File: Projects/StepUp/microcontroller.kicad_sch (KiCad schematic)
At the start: 34 parts, among them J1 USB_C_Receptacle_USB2.0_16P, J2 Conn_01x02, J3 Conn_02x03_Odd_Even, J4 Conn_02x06_Odd_Even, SW1 FSM8JSMASTR, SW2 FSM8JSMASTR, SW3 FSM8JSMASTR, U1 USBLC6-2SC6, U2 W25Q128JVS, U3 RP2040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

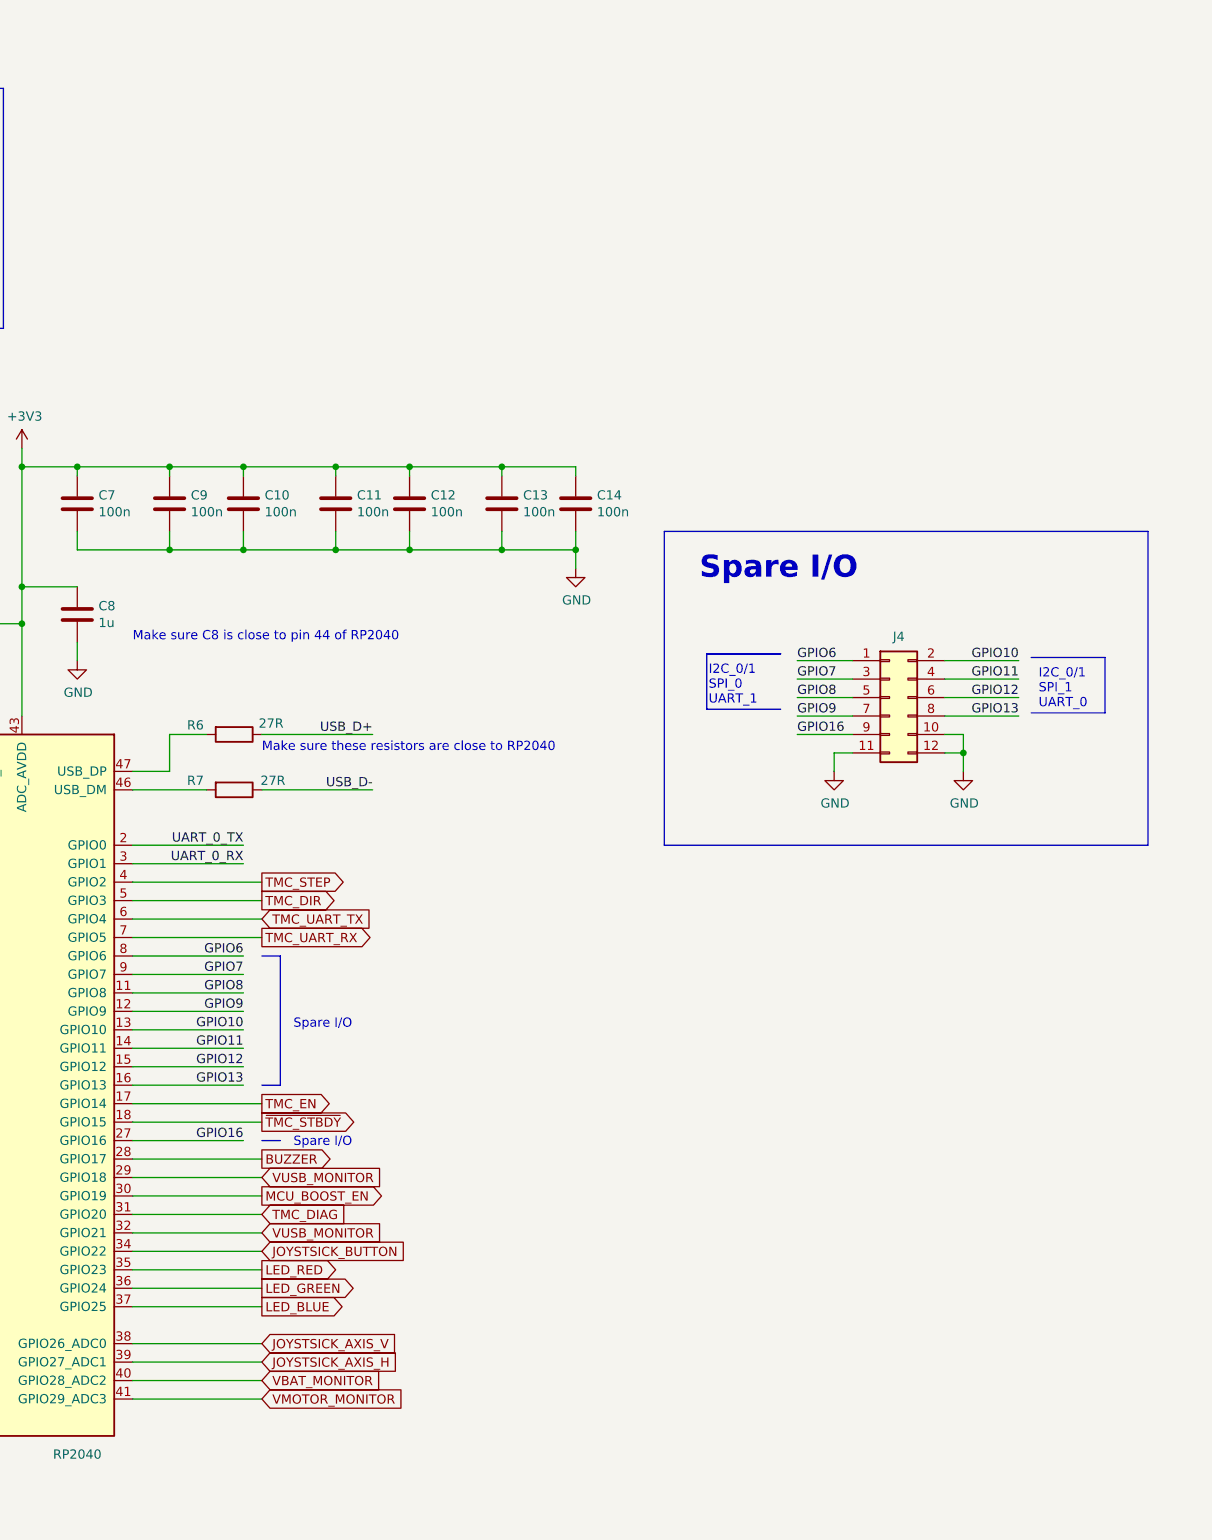
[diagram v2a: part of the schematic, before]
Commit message: feat(layout): DRC ongoing, layout nearly complete
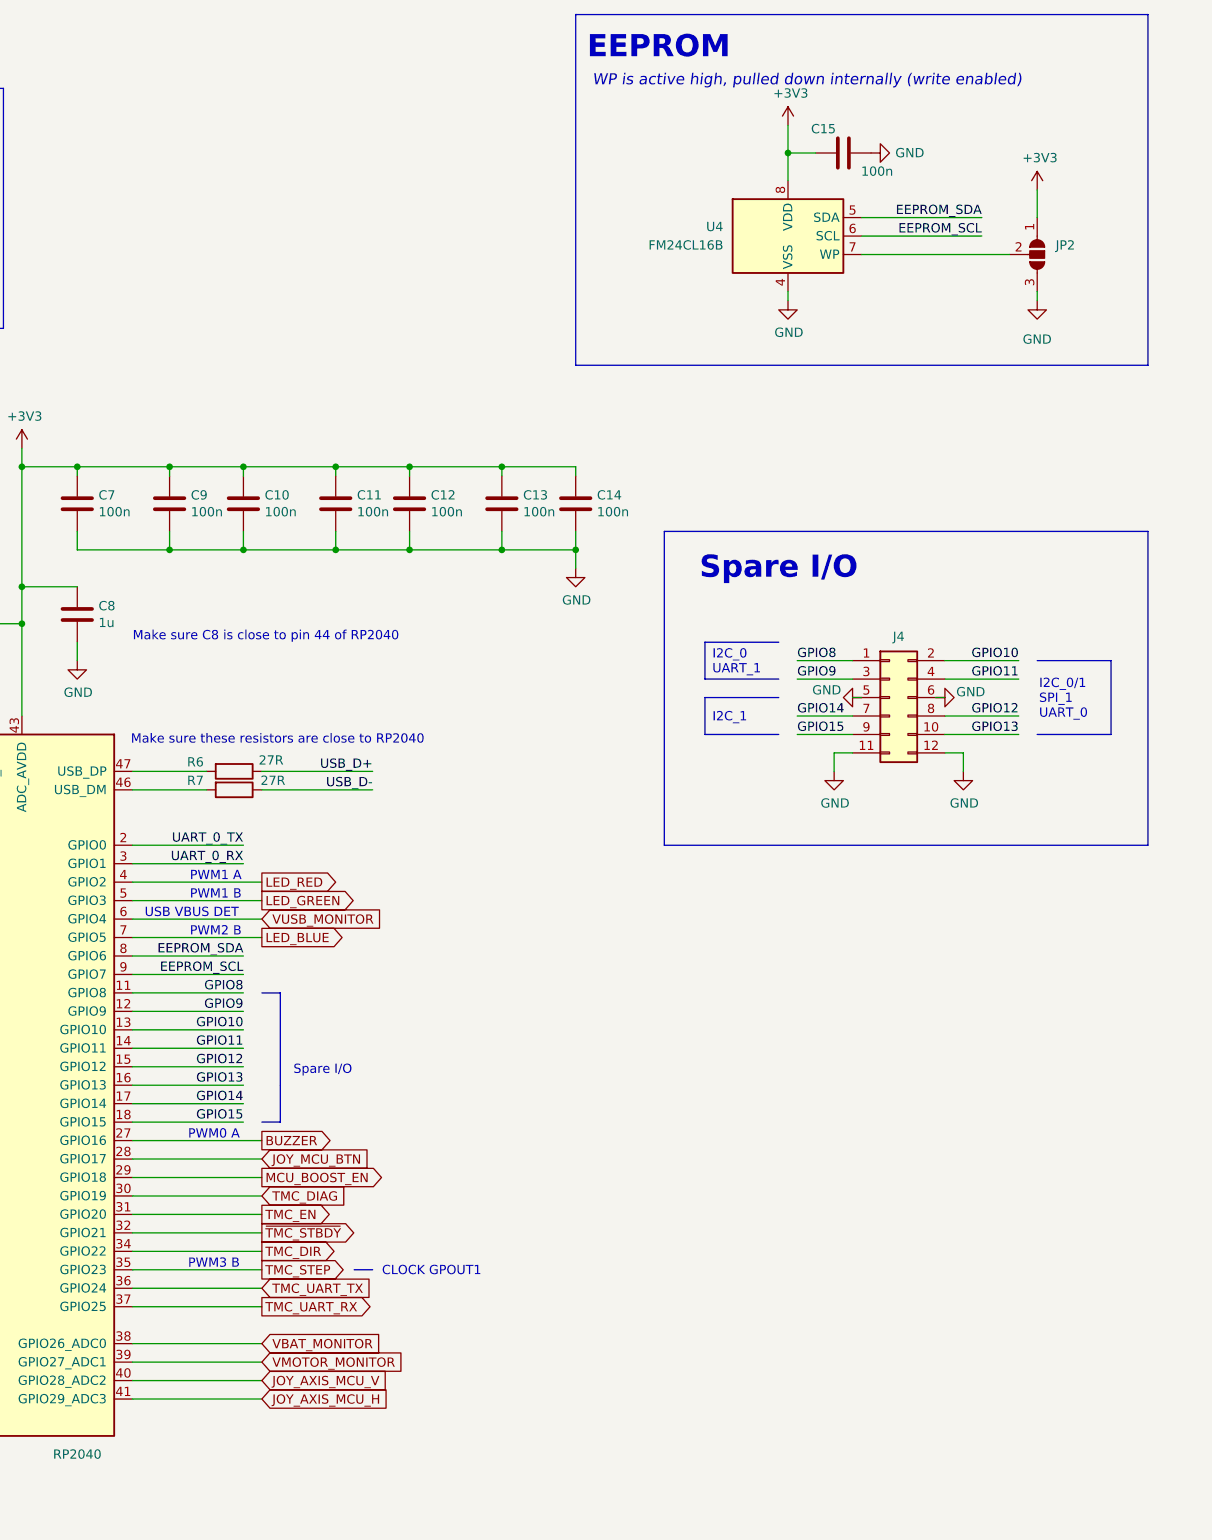
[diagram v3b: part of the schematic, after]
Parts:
- added C15: 100n, Capacitor_SMD:C_0402_1005Metric, symbol Device:C
- added JP2: SolderJumper_3_Open, Jumper:SolderJumper-3_P1.3mm_Bridged12_RoundedPad1.0x1.5mm, symbol Jumper:SolderJumper_3_Open
- added U4: FM24CL16B, Package_SO:SOIC-8_3.9x4.9mm_P1.27mm, symbol Memory_NVRAM:FM24CL16B
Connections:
- net JOYSTSICK_AXIS_H is gone; now on net VMOTOR_MONITOR: U3.39 (GPIO27_ADC1)
- net JOYSTSICK_AXIS_V is gone; now on net VBAT_MONITOR: U3.38 (GPIO26_ADC0)
- net JOYSTSICK_BUTTON is gone; now on net TMC_DIR: U3.34 (GPIO22)
- net +3V3: now also C15.1, JP2.1 (A), U4.8 (VDD)
- net BUZZER: now also U3.27 (GPIO16); no longer U3.28 (GPIO17)
- net GND: now also J4.5 (Pin_5), J4.6 (Pin_6), C15.2, JP2.3 (B), U4.4 (VSS); no longer J4.10 (Pin_10)
- net GPIO12: now also J4.8 (Pin_8); no longer J4.6 (Pin_6)
- net GPIO13: now also J4.10 (Pin_10); no longer J4.8 (Pin_8)
- net GPIO8: now also J4.1 (Pin_1); no longer J4.5 (Pin_5)
- net GPIO9: now also J4.3 (Pin_3); no longer J4.7 (Pin_7)
- net LED_BLUE: now also U3.7 (GPIO5); no longer U3.37 (GPIO25)
- net LED_GREEN: now also U3.5 (GPIO3); no longer U3.36 (GPIO24)
- net LED_RED: now also U3.4 (GPIO2); no longer U3.35 (GPIO23)
- net MCU_BOOST_EN: now also U3.29 (GPIO18); no longer U3.30 (GPIO19)
- net TMC_DIAG: now also U3.30 (GPIO19); no longer U3.31 (GPIO20)
- net TMC_DIR: no longer U3.5 (GPIO3)
- net TMC_EN: now also U3.31 (GPIO20); no longer U3.17 (GPIO14)
- net TMC_STEP: now also U3.35 (GPIO23); no longer U3.4 (GPIO2)
- net TMC_UART_RX: now also U3.37 (GPIO25); no longer U3.7 (GPIO5)
- net TMC_UART_TX: now also U3.36 (GPIO24); no longer U3.6 (GPIO4)
- net VBAT_MONITOR: no longer U3.40 (GPIO28_ADC2)
- net VMOTOR_MONITOR: no longer U3.41 (GPIO29_ADC3)
- net VUSB_MONITOR: now also U3.6 (GPIO4); no longer U3.29 (GPIO18), U3.32 (GPIO21)
- net ~{TMC_STBDY}: now also U3.32 (GPIO21); no longer U3.18 (GPIO15)
- net GPIO16 renamed GPIO15
- net GPIO15: now also U3.18 (GPIO15); no longer U3.27 (GPIO16)
- net GPIO6 renamed EEPROM_SDA
- net EEPROM_SDA: now also U4.5 (SDA); no longer J4.1 (Pin_1)
- net GPIO7 renamed EEPROM_SCL
- net EEPROM_SCL: now also U4.6 (SCL); no longer J4.3 (Pin_3)
- new net: JP2.2 (C), U4.7 (WP)
- new net GPIO14: J4.7 (Pin_7), U3.17 (GPIO14)
- new net JOY_AXIS_MCU_H: U3.41 (GPIO29_ADC3)
- new net JOY_AXIS_MCU_V: U3.40 (GPIO28_ADC2)
- new net JOY_MCU_BTN: U3.28 (GPIO17)
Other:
- note added: "CLOCK GPOUT1"
- note added: "EEPROM"
- note added: "I2C_0 UART_1"
- note added: "I2C_1"
- note added: "PWM0 A"
- note added: "PWM1 A"
- note added: "PWM1 B"
- note added: "PWM2 B"
- note added: "PWM3 B"
- note added: "USB VBUS DET"
- note added: "WP is active high, pulled down internally (write enabled)"
- note removed: "I2C_0/1 SPI_0 UART_1"
- moved on the sheet: R6

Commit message: feat(StepUp): Release v0.1
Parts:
- added R8, R9: 10kR, Resistor_SMD:R_0603_1608Metric, symbol Device:R
- C1, C2: value 15p -> 15pF; Package (none) -> 0402; Type (none) -> SMD
- C10, C11, C12, C13, C3, C4, C5, C7, C9: value 100n -> 100nF; Package (none) -> 0402; Type (none) -> SMD; Voltage (none) -> 25V
- C14: renamed from C15; value 100n -> 100nF; Package (none) -> 0402; Type (none) -> SMD; Voltage (none) -> 25V
- C15: renamed from C14; value 100n -> 100nF; Package (none) -> 0402; Type (none) -> SMD; Voltage (none) -> 25V
- C6, C8: value 1u -> 1uF; Package (none) -> 0402; Type (none) -> SMD
- D1: MF (none) -> Micro Commercial Co; Type (none) -> SMD
- J1: MPN (none) -> USB4105-GF-A; Manufacturer (none) -> GCT; Type (none) -> SMD/thru-hole
- J2, J3, J4, JP1, JP2, R2: now not fitted
- R1, R5, R6, R7: Package (none) -> 0402; Tolerance (none) -> 1%; Type (none) -> SMD
- R3, R4: Package (none) -> 0603; Tolerance (none) -> 1%; Type (none) -> SMD
- SW1, SW2, SW3: MPN (none) -> FSM8JSMASTR; Manufacturer (none) -> TE Connectivity ALCOSWITCH Switches; Type (none) -> thru-hole
- U1: MPN (none) -> USBLC6-2SC6; Manufacturer (none) -> STMicroelectronics; Type (none) -> SMD
- U2: MPN (none) -> W25Q128JVSIQ; Manufacturer (none) -> Winbond Electronics; Type (none) -> SMD
- U3: MPN (none) -> RP2040; Manufacturer (none) -> Raspberry Pi; Type (none) -> SMD
- U4: MPN (none) -> FM24CL16B-G; Manufacturer (none) -> Infineon Technologies; Type (none) -> SMD
- Y1: MPN (none) -> ABM8-272-T3; Manufacturer (none) -> Abracon LLC; Type (none) -> SMD
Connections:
- net +3V3: now also R8.2, R9.2
- net EEPROM_SCL: now also R8.1
- net EEPROM_SDA: now also R9.1
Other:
- company: Samio -> SJFOM
- moved on the sheet: C14, U4

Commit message: feat(BoM): Updating PN's
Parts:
- C6, C8: MPN (none) -> GRM155R61E105MA12D; Manufacturer (none) -> Murata Electronics
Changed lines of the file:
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@@
 			)
 		)
+		(property "MPN" "GRM155R61E105MA12D"
+			(at 238.76 100.33 0)
+			(effects
+				(font
+					(size 1.27 1.27)
+				)
+				(hide yes)
+			)
+		)
+		(property "Manufacturer" "Murata Electronics"
+			(at 238.76 100.33 0)
+			(effects
+				(font
+					(size 1.27 1.27)
+				)
+				(hide yes)
+			)
+		)
 		(pin "1"
 		)
@@
 			(at 185.42 100.33 0)
 			(effects
+				(font
+					(size 1.27 1.27)
+				)
+				(hide yes)
+			)
+		)
+		(property "MPN" "GRM155R61E105MA12D"
+			(at 185.42 100.33 0)
+			(effects
+				(font
+					(size 1.27 1.27)
+				)
+				(hide yes)
+			)
+		)
+		(property "Manufacturer" "Murata Electronics"
+			(at 185.42 100.33 0)
+			(effects

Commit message: chore(bom): Update from PCB BoM
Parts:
- C1, C2: Dielectric (none) -> C0G, NP0; MPN (none) -> CC0402FRNPO9BN150; Manufacturer (none) -> YAGEO; Tolerance (none) -> 1%; Voltage (none) -> 50V
- C10, C11, C12, C13, C14, C15, C3, C4, C5, C7, C9: Dielectric (none) -> X7R; MPN (none) -> CC0402KRX7R8BB104; Manufacturer (none) -> YAGEO; Tolerance (none) -> 10%
- C6, C8: Dielectric (none) -> X5R; Tolerance (none) -> 20%; Voltage (none) -> 25V
- R1, R5: MPN (none) -> RC0402FR-071KL; Manufacturer (none) -> YAGEO; Power (none) -> 0.063W, 1/16W
- R3, R4: MPN (none) -> RC0603FR-075K1L; Manufacturer (none) -> YAGEO; Power (none) -> 0.063W, 1/16W
- R6, R7: MPN (none) -> RC0402FR-0727RL; Manufacturer (none) -> YAGEO; Power (none) -> 0.063W, 1/16W
- R8, R9: MPN (none) -> RC0603FR-0710KL; Manufacturer (none) -> YAGEO; Power (none) -> 0.1W, 1/10W

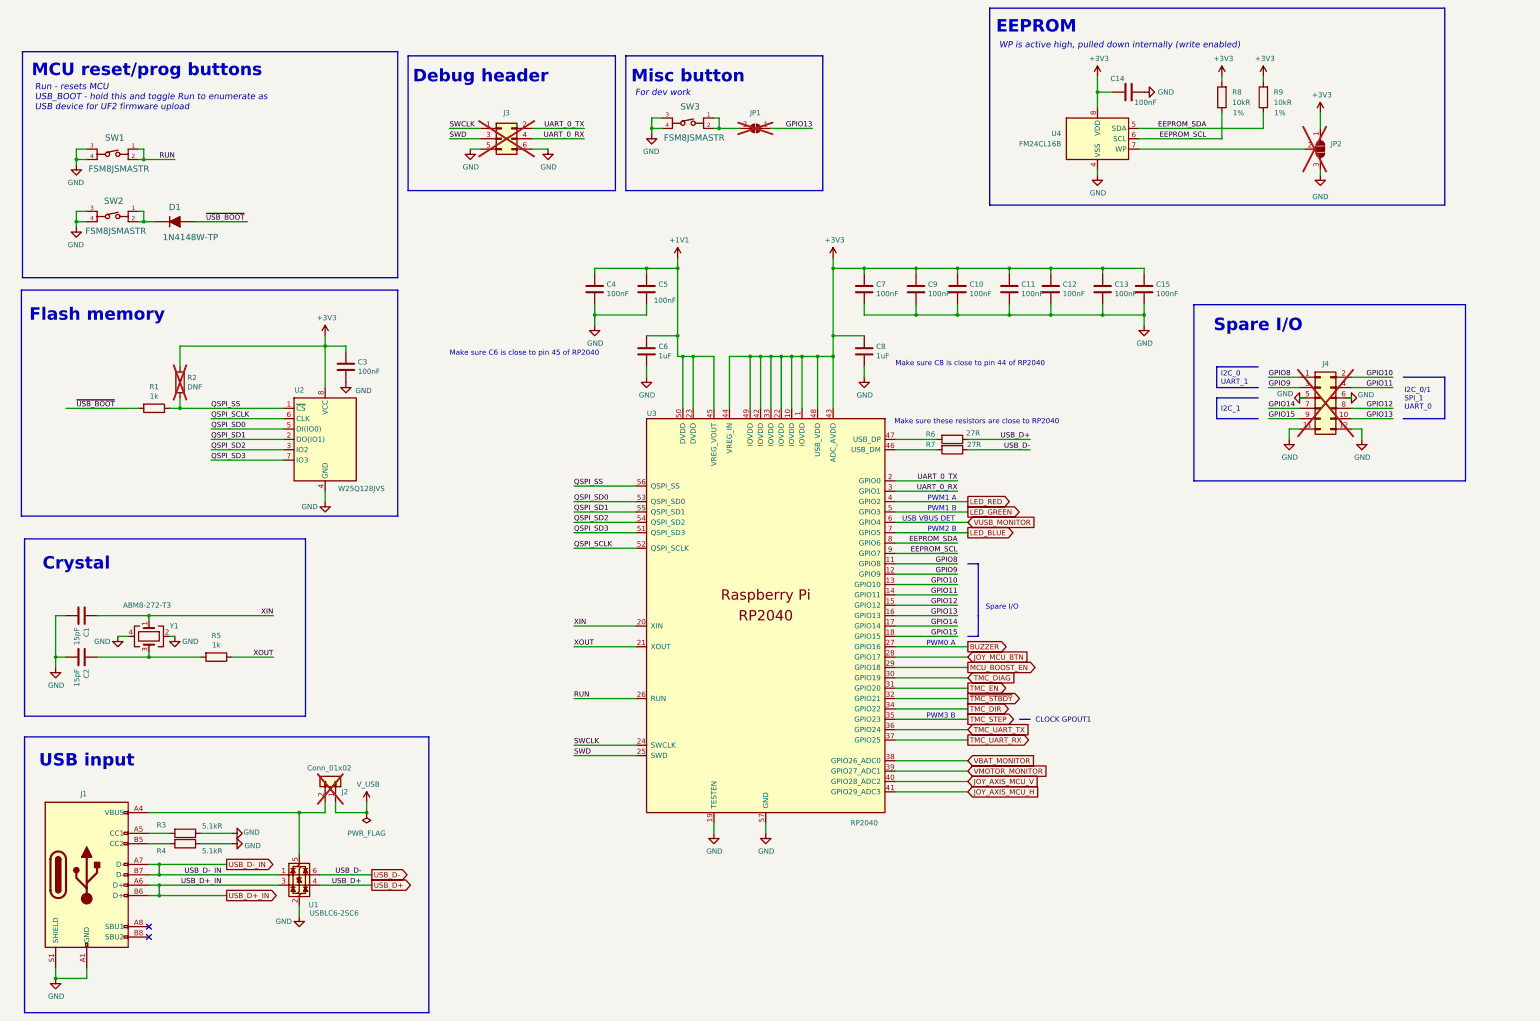
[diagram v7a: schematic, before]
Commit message: feat(v0.2): Schematic updated, PCB layout start
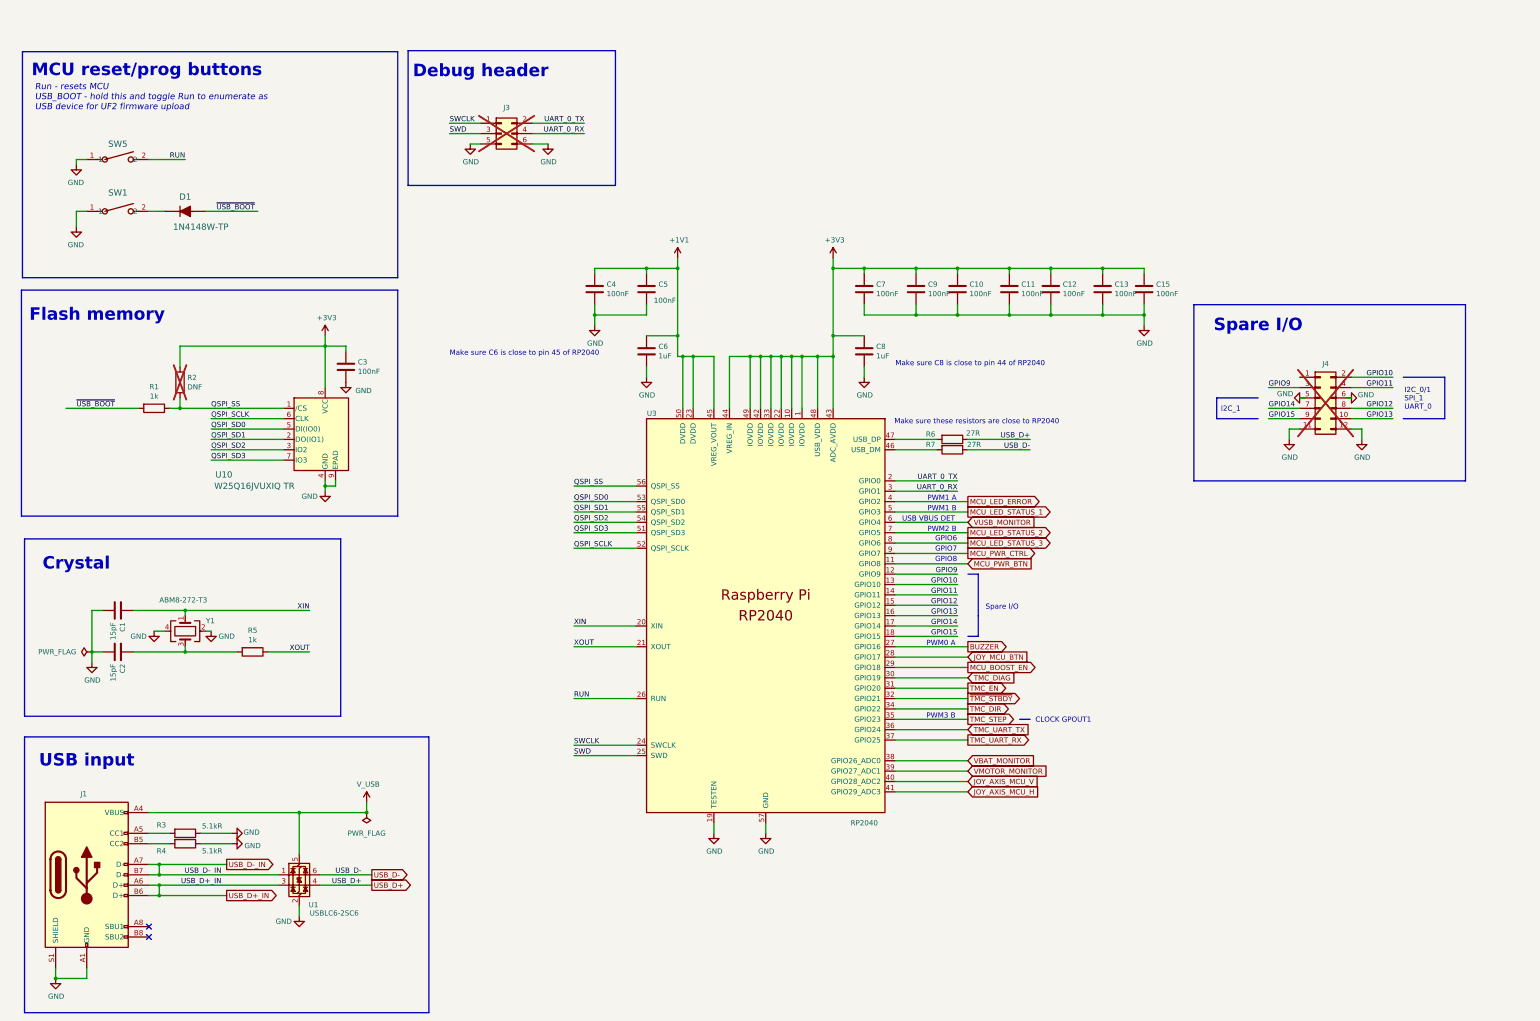
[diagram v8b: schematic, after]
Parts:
- removed C14: 100nF, Capacitor_SMD:C_0402_1005Metric, symbol Device:C
- removed J2: Conn_01x02, Connector_PinHeader_2.54mm:PinHeader_1x02_P2.54mm_Vertical, symbol Connector_Generic:Conn_01x02
- removed JP1: SolderJumper_2_Open, Jumper:SolderJumper-2_P1.3mm_Open_RoundedPad1.0x1.5mm, symbol Jumper:SolderJumper_2_Open
- removed JP2: SolderJumper_3_Open, Jumper:SolderJumper-3_P1.3mm_Bridged12_RoundedPad1.0x1.5mm, symbol Jumper:SolderJumper_3_Open
- removed R8, R9: 10kR, Resistor_SMD:R_0603_1608Metric, symbol Device:R
- removed SW1, SW2, SW3: FSM8JSMASTR, Snapeda:SW4_FSM8JSMASTR_TEC, symbol Snapeda_kicad_2:FSM8JSMASTR
- removed U2: W25Q128JVS, Package_SO:SOIC-8_5.23x5.23mm_P1.27mm, symbol Memory_Flash:W25Q128JVS
- removed U4: FM24CL16B, Package_SO:SOIC-8_3.9x4.9mm_P1.27mm, symbol Memory_NVRAM:FM24CL16B
- added SW1, SW5: PTS636SL43SMTRLFS, Snapeda:SW_PTS636S-J_CNK, symbol Snapeda_kicad:PTS636SL43SMTRLFS
- added U10: W25Q16JVUXIQ TR, Snapeda:USON-8_UX_2x3x0p6_WIN, symbol Snapeda_kicad:W25Q16JVUXIQ_TR
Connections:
- net +3V3: now also U10.8 (VCC)
- net GND: now also SW1.1, SW5.1, U10.4 (GND), U10.9 (EPAD)
- net QSPI_SCLK: now also U10.6 (CLK)
- net QSPI_SD0: now also U10.5 (DI(IO0))
- net QSPI_SD1: now also U10.2 (DO(IO1))
- net QSPI_SD2: now also U10.3 (IO2)
- net QSPI_SD3: now also U10.7 (IO3)
- net QSPI_SS: now also U10.1 (/CS)
- net RUN: now also SW5.2
- net V_USB: now also J1.A4 (VBUS), J1.A9 (VBUS), J1.B4 (VBUS), J1.B9 (VBUS), U1.5 (VBUS)
- net at D1.K: now also SW1.2
- net EEPROM_SCL renamed MCU_PWR_CTRL
- net EEPROM_SDA renamed MCU_LED_STATUS_3
- net GPIO8: no longer names the net of J4.1 (Pin_1)
- net GPIO8: no longer U3.11 (GPIO8)
- net LED_BLUE renamed MCU_LED_STATUS_2
- net LED_GREEN renamed MCU_LED_STATUS_1
- net LED_RED renamed MCU_LED_ERROR
- new net MCU_PWR_BTN: U3.11 (GPIO8)
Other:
- note added: "GPIO6"
- note added: "GPIO7"
- note added: "GPIO8"
- note removed: "EEPROM"
- note removed: "For dev work"
- note removed: "I2C_0 UART_1"
- note removed: "Misc button"
- note removed: "WP is active high, pulled down internally (write enabled)"
- moved on the sheet: C1, C2, J3, R5, Y1
